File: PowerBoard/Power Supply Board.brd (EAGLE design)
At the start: 65.4 x 76.2 mm, 37 parts, among them IC3 LM2675

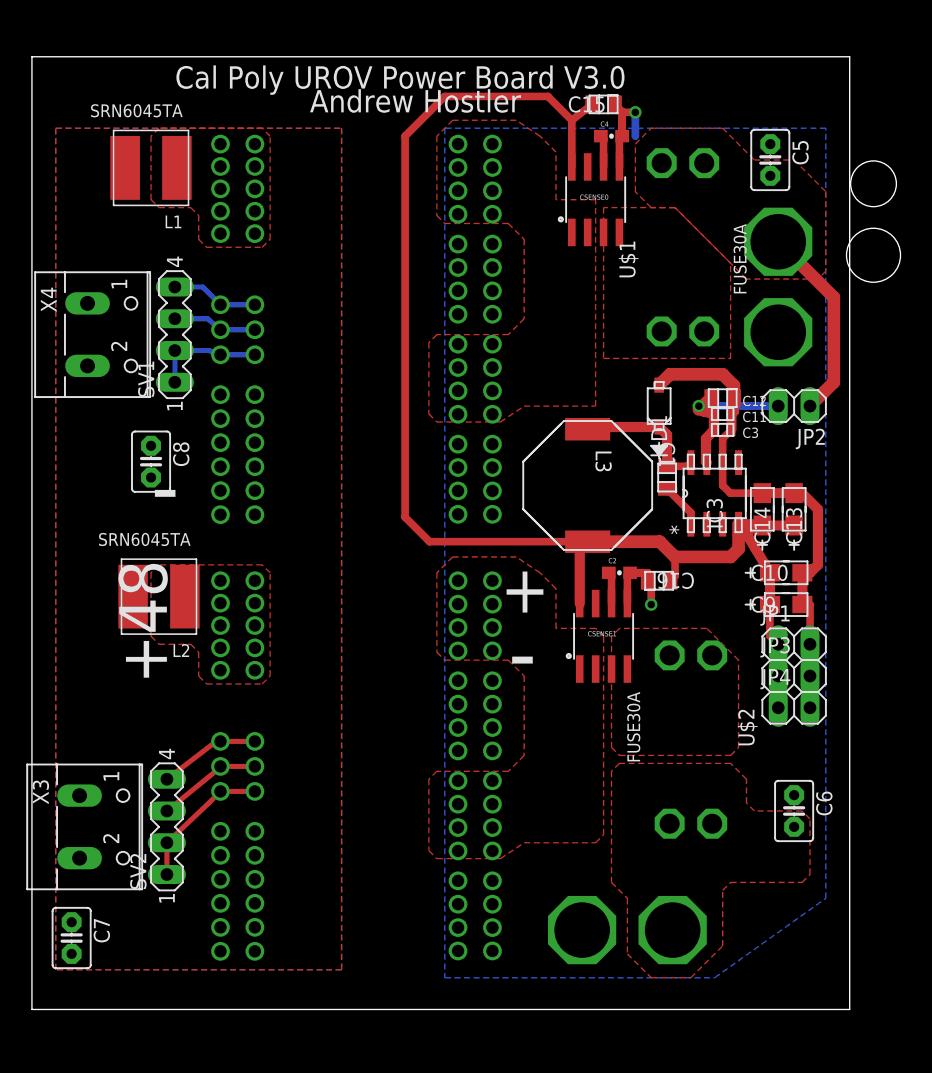
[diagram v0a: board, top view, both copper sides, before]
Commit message: Power Supply Board changes
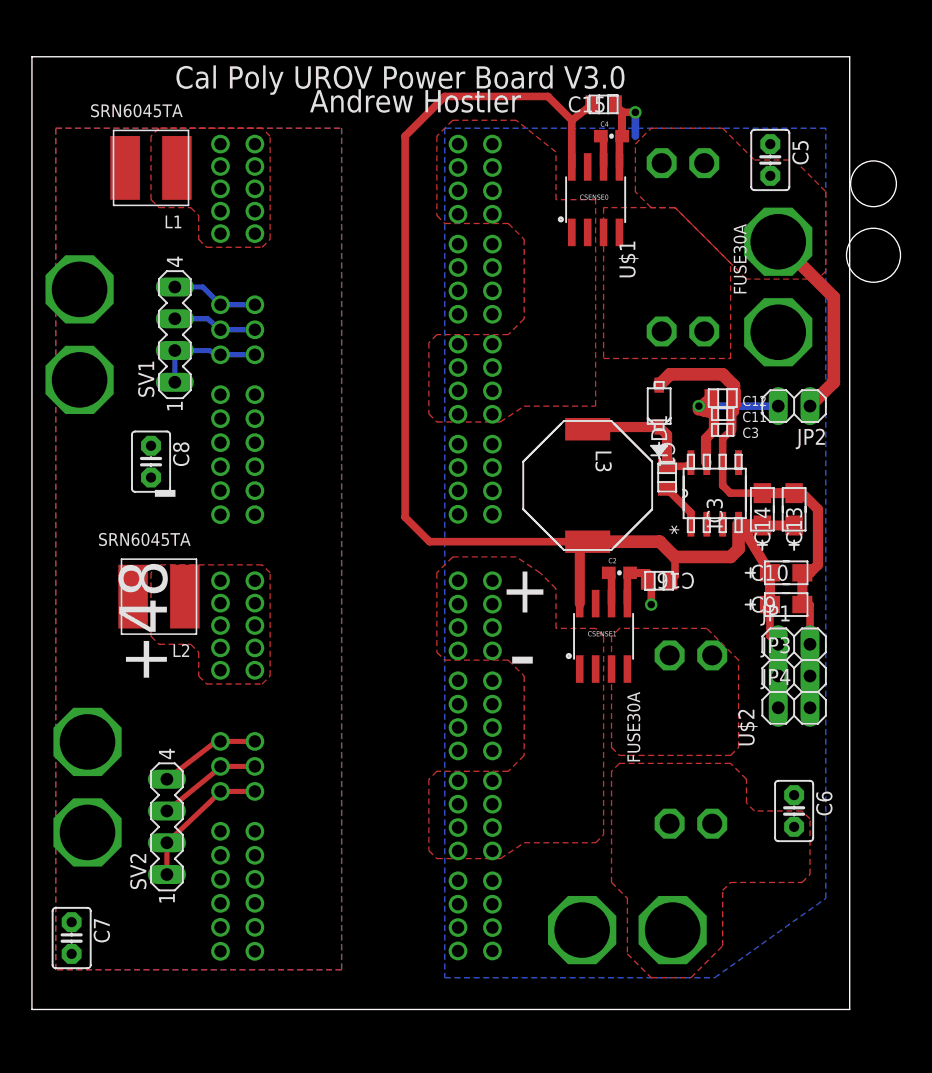
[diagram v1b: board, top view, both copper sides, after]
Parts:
- removed X3, X4: (no value), con-wago-500:W237-102
- added U$5, U$6: XT60, HostlerLib:XT60
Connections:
- net 48V+: now also U$5.P$2, U$6.P$2; no longer X3.1, X4.1
- net 48V-: now also U$5.P$1, U$6.P$1; no longer X3.2, X4.2
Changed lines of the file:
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@@
 </element>
 <element name="C6" library="capacitor-wima" package="C2.5-3" value="" x="60.96" y="15.875" rot="R270"/>
-<element name="X3" library="con-wago-500" package="W237-102" value="" x="5.08" y="14.605" rot="R270">
-<attribute name="OC_FARNELL" value="unknown" x="17.145" y="24.765" size="1.778" layer="27" rot="R270" display="off"/>
-<attribute name="MF" value="" x="17.145" y="24.765" size="1.778" layer="27" rot="R270" display="off"/>
-<attribute name="MPN" value="237-102" x="17.145" y="24.765" size="1.778" layer="27" rot="R270" display="off"/>
-<attribute name="OC_NEWARK" value="70K9898" x="17.145" y="24.765" size="1.778" layer="27" rot="R270" display="off"/>
-</element>
-<element name="X4" library="con-wago-500" package="W237-102" value="" x="5.715" y="53.975" rot="R270">
-<attribute name="OC_FARNELL" value="unknown" x="18.415" y="64.135" size="1.778" layer="27" rot="R270" display="off"/>
-<attribute name="MF" value="" x="18.415" y="64.135" size="1.778" layer="27" rot="R270" display="off"/>
-<attribute name="MPN" value="237-102" x="18.415" y="64.135" size="1.778" layer="27" rot="R270" display="off"/>
-<attribute name="OC_NEWARK" value="70K9898" x="18.415" y="64.135" size="1.778" layer="27" rot="R270" display="off"/>
-</element>
 <element name="C7" library="capacitor-wima" package="C2.5-3" value="" x="3.175" y="5.715" rot="R270"/>
 <element name="C8" library="capacitor-wima" package="C2.5-3" value="" x="9.525" y="43.815" rot="R270"/>
@@
 <element name="JP3" library="pinhead" package="1X02" value="" x="60.96" y="26.67"/>
 <element name="JP4" library="pinhead" package="1X02" value="" x="60.96" y="24.13"/>
+<element name="U$5" library="HostlerLib" package="XT60" value="XT60" x="4.445" y="17.78" rot="R90"/>
+<element name="U$6" library="HostlerLib" package="XT60" value="XT60" x="3.81" y="53.975" rot="R90"/>
 </elements>
 <signals>
@@
 <contactref element="C7" pad="1"/>
 <contactref element="C8" pad="1"/>
-<contactref element="X3" pad="1"/>
-<contactref element="X4" pad="1"/>
 <contactref element="L1" pad="P$1"/>
 <contactref element="L2" pad="P$1"/>
+<contactref element="U$5" pad="P$2"/>
+<contactref element="U$6" pad="P$2"/>
+<wire x1="7.4549" y1="67.31" x2="3.81" y2="57.5945" width="0" layer="19" extent="1-1"/>
 </signal>
 <signal name="48V-">
@@
 <contactref element="C7" pad="2"/>
 <contactref element="C8" pad="2"/>
-<contactref element="X3" pad="2"/>
-<contactref element="X4" pad="2"/>
+<contactref element="U$5" pad="P$1"/>
+<contactref element="U$6" pad="P$1"/>
+<wire x1="9.525" y1="42.545" x2="3.81" y2="50.3555" width="0" layer="19" extent="1-1"/>
 </signal>
 <signal name="48VIN1">
@@
 <vertex x="41.91" y="64.77"/>
 <vertex x="41.91" y="68.58"/>
-<vertex x="40.64" y="69.85"/>
 <vertex x="38.735" y="71.12"/>
 </polygon>

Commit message: Power board updates
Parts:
- moved U$5 2.54 mm to (4.45, 20.3)
- moved U$6 1.42 mm to (4.45, 55.2)
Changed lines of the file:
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@@
 <element name="JP3" library="pinhead" package="1X02" value="" x="60.96" y="26.67"/>
 <element name="JP4" library="pinhead" package="1X02" value="" x="60.96" y="24.13"/>
-<element name="U$5" library="HostlerLib" package="XT60" value="XT60" x="4.445" y="17.78" rot="R90"/>
-<element name="U$6" library="HostlerLib" package="XT60" value="XT60" x="3.81" y="53.975" rot="R90"/>
+<element name="U$5" library="HostlerLib" package="XT60" value="XT60" x="4.445" y="20.32" rot="R90"/>
+<element name="U$6" library="HostlerLib" package="XT60" value="XT60" x="4.445" y="55.245" rot="R90"/>
 </elements>
 <signals>
@@
 <contactref element="U$5" pad="P$2"/>
 <contactref element="U$6" pad="P$2"/>
-<wire x1="7.4549" y1="67.31" x2="3.81" y2="57.5945" width="0" layer="19" extent="1-1"/>
 </signal>
 <signal name="48V-">
@@
 <contactref element="U$5" pad="P$1"/>
 <contactref element="U$6" pad="P$1"/>
-<wire x1="9.525" y1="42.545" x2="3.81" y2="50.3555" width="0" layer="19" extent="1-1"/>
 </signal>
 <signal name="48VIN1">

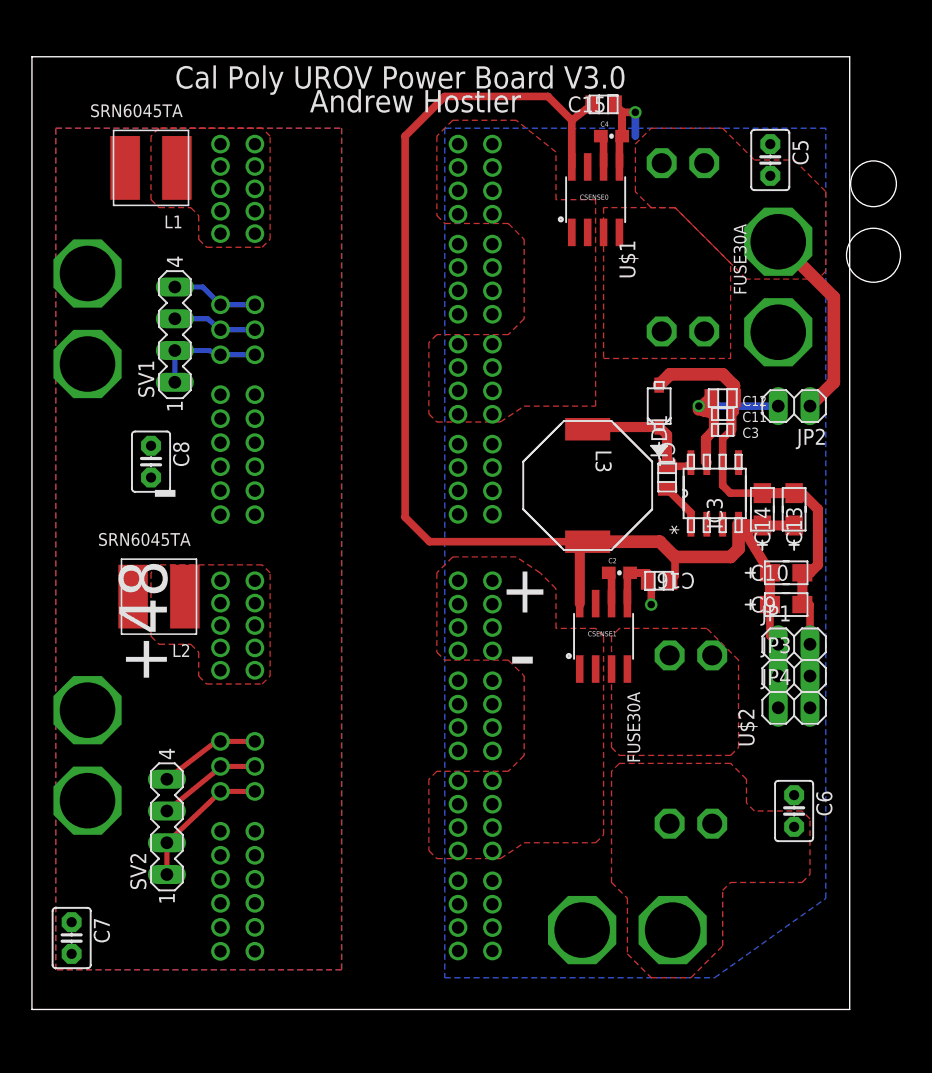
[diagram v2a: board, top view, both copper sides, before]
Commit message: Power Supply Labeling
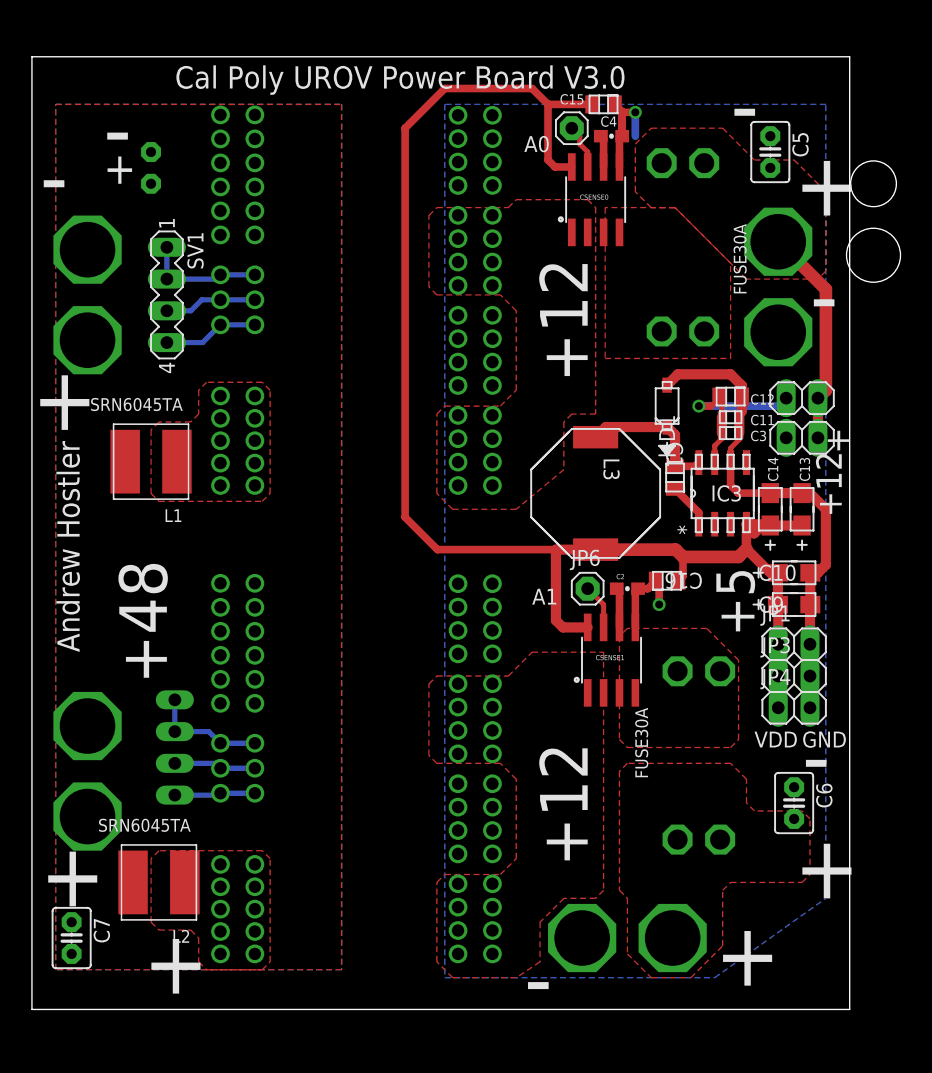
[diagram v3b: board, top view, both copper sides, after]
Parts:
- added JP5, JP6: (no value), adafruit:1X01
- added JP7: (no value), pinhead:1X02
- moved VC2 29.8 mm to (36.8, 4.45), flipped to the bottom, turned to 180 degrees
- moved VC1 27.3 mm to (36.8, 41.9), flipped to the bottom, turned to 180 degrees
- moved C8 23.5 mm to (9.53, 67.3), flipped to the bottom, turned to 90 degrees
- moved L1 23.5 mm to (9.53, 43.8)
- moved L2 22.9 mm to (10.2, 10.2)
- moved SV2 6.38 mm to (11.4, 21.0), flipped to the bottom, turned to 270 degrees
- moved SV1 3.24 mm to (10.8, 57.1), turned to 270 degrees
- moved CSENSE1 2.01 mm to (46.4, 27.9)
- moved U$6 1.91 mm to (4.45, 57.1), flipped to the bottom, turned to 270 degrees
- moved U$2 1.42 mm to (53.3, 20.3)
- moved C2 1.42 mm to (47.6, 33.7)
- moved U$5 1.27 mm to (4.45, 19.1), turned to 270 degrees
- moved JP2 0.90 mm to (61.6, 48.9)
- moved L3 0.90 mm to (45.1, 41.3)
- moved C11 0.68 mm to (55.9, 47.4)
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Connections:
- net A0: now also JP5.1
- net A1: now also JP6.1
- net GROUNDOUT: now also JP7.2
- net POWER_BANK_0: now also JP7.1
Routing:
- net 5V: track 111.0 -> 117.0 mm
- net A1: track 0.00 -> 3.62 mm
- net A0: track 0.00 -> 3.62 mm
- net PC2: track 11.2 -> 9.33 mm
- net N$5: track 8.33 -> 6.56 mm
- net POWER_BANK_0: track 15.8 -> 17.5 mm
- net GROUNDOUT: track 59.5 -> 57.8 mm
- net TM2: track 8.18 -> 6.46 mm
- net PC1: track 9.00 -> 9.72 mm
- net N$2: track 6.73 -> 7.40 mm
- net V12: track 14.2 -> 14.9 mm
- net FILT2: track 2.55 -> 3.19 mm
- net TM1: track 6.99 -> 7.62 mm
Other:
- board text added: "+12"
- board text added: "+5"
- board text added: "A0"
- board text added: "A1"
- board text added: "GND"
- board text added: "VDD"
- board text removed: "GND IN"

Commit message: slight routing additions
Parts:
- added JP8: (no value), pinhead:1X02
- moved JP2 4.45 mm to (61.6, 53.3)
- moved JP7 4.45 mm to (61.6, 50.2)
- moved U$3 4.45 mm to (59.7, 62.2)
- moved C5 3.17 mm to (59.1, 71.8)
- moved U$6 1.42 mm to (3.81, 58.4)
- moved U$5 1.42 mm to (3.81, 20.3)
- moved C4 1.27 mm to (46.4, 71.1)
- moved CSENSE0 1.27 mm to (45.1, 66.0)
- moved C10 1.27 mm to (61.0, 36.2)
- moved C12 1.27 mm to (55.9, 50.3)
- moved C16 1.27 mm to (50.8, 35.6)
- moved C3 1.27 mm to (55.9, 47.4)
- moved C9 1.27 mm to (61.0, 33.7)
- moved D1 1.27 mm to (50.8, 49.5)
- moved IC3 1.27 mm to (55.2, 42.5)
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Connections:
- net GROUNDOUT: now also JP8.2
- net POWER_BANK_0: now also JP8.1
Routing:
- net POWER_BANK_0: track 17.5 -> 21.2 mm
- net V12: track 14.9 -> 16.2 mm
- net GROUNDOUT: track 57.8 -> 59.1 mm
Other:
- board size 65.4 x 76.2 mm -> 65.4 x 78.7 mm
- board text added: "Cal Poly UROV"
- board text added: "Power Board V3.0"

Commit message: Power gerber generated
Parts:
- moved JP8 1.27 mm to (61.6, 48.3)
- moved JP7 0.63 mm to (61.6, 50.8)
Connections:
- removed net PC2: SV2.1, SV2.2, VC2.PC, VC2.PC21
- net PC1: now also SV2.1, SV2.2, VC2.PC, VC2.PC21
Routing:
- net PC1: track 9.72 -> 73.4 mm
- net PC2: track 9.33 -> 0.00 mm
- net POWER_BANK_0: track 21.2 -> 20.0 mm

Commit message: final changes for FAB
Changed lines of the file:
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@@
 <hole x="62.865" y="76.2" drill="2.8448"/>
 <hole x="62.865" y="2.54" drill="2.8448"/>
-<hole x="2.79" y="2.54" drill="2.8448"/>
+<hole x="2.54" y="2.54" drill="2.8448"/>
 <hole x="2.54" y="39.37" drill="2.8448"/>
 <text x="5.08" y="3.175" size="3.81" layer="25">-</text>
